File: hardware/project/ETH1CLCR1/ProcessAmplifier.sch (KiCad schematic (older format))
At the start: 87 parts, among them Q901 BC847W, Q902 BC847W, Q903 BC847W, U901 TL072, U902 TL072, U903 TL072, U904 TL072, U905 TL071, U906 TL071, U907 AQY212GS, U908 AQY212GS, U909 AQY212GS, U910 AQY212GS, U911 AQY212GS, U912 AQY212GS, U913 AQY212GS, U914 AQY212GS, U915 AQY212GS, U916 AQY212GS, U917 ULN2003A

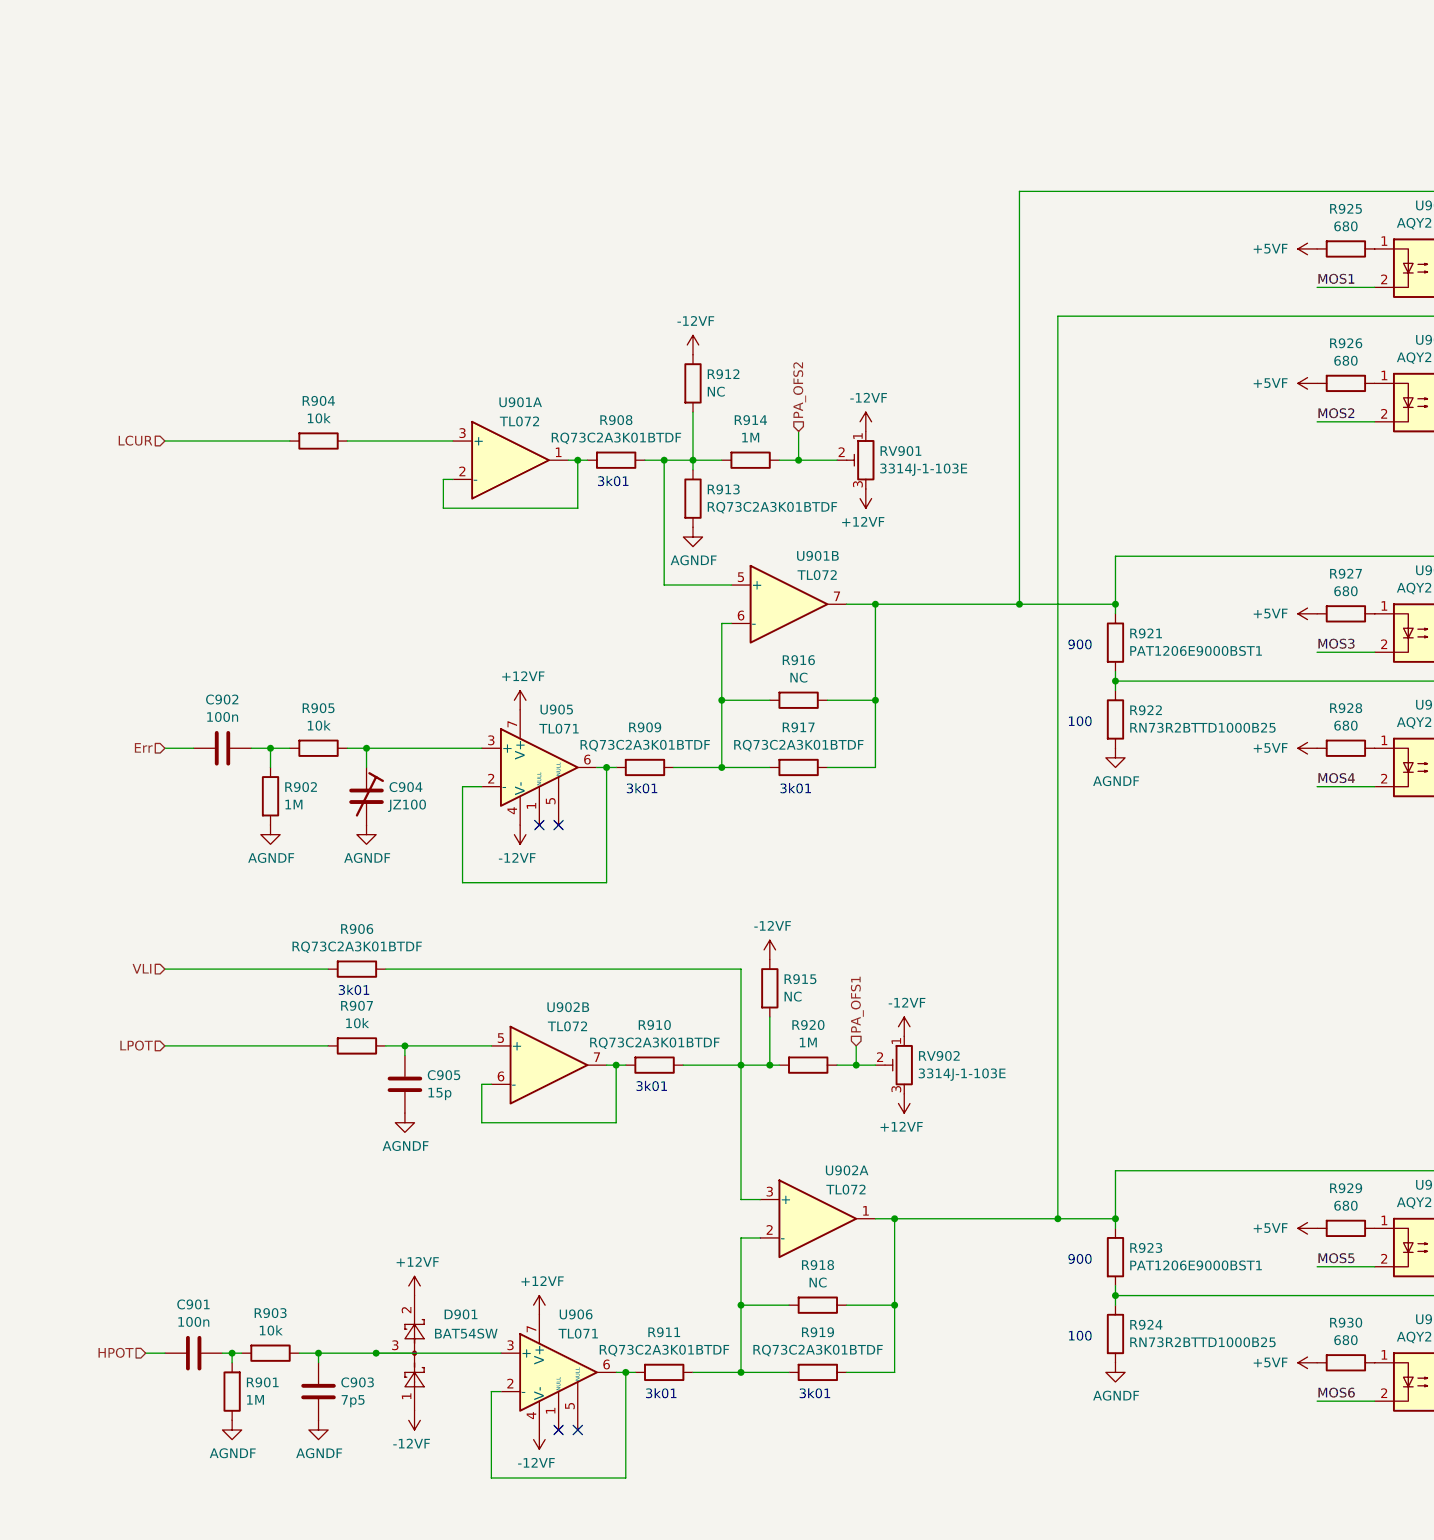
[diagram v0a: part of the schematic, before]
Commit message: Checked the schematics. Created BOM.
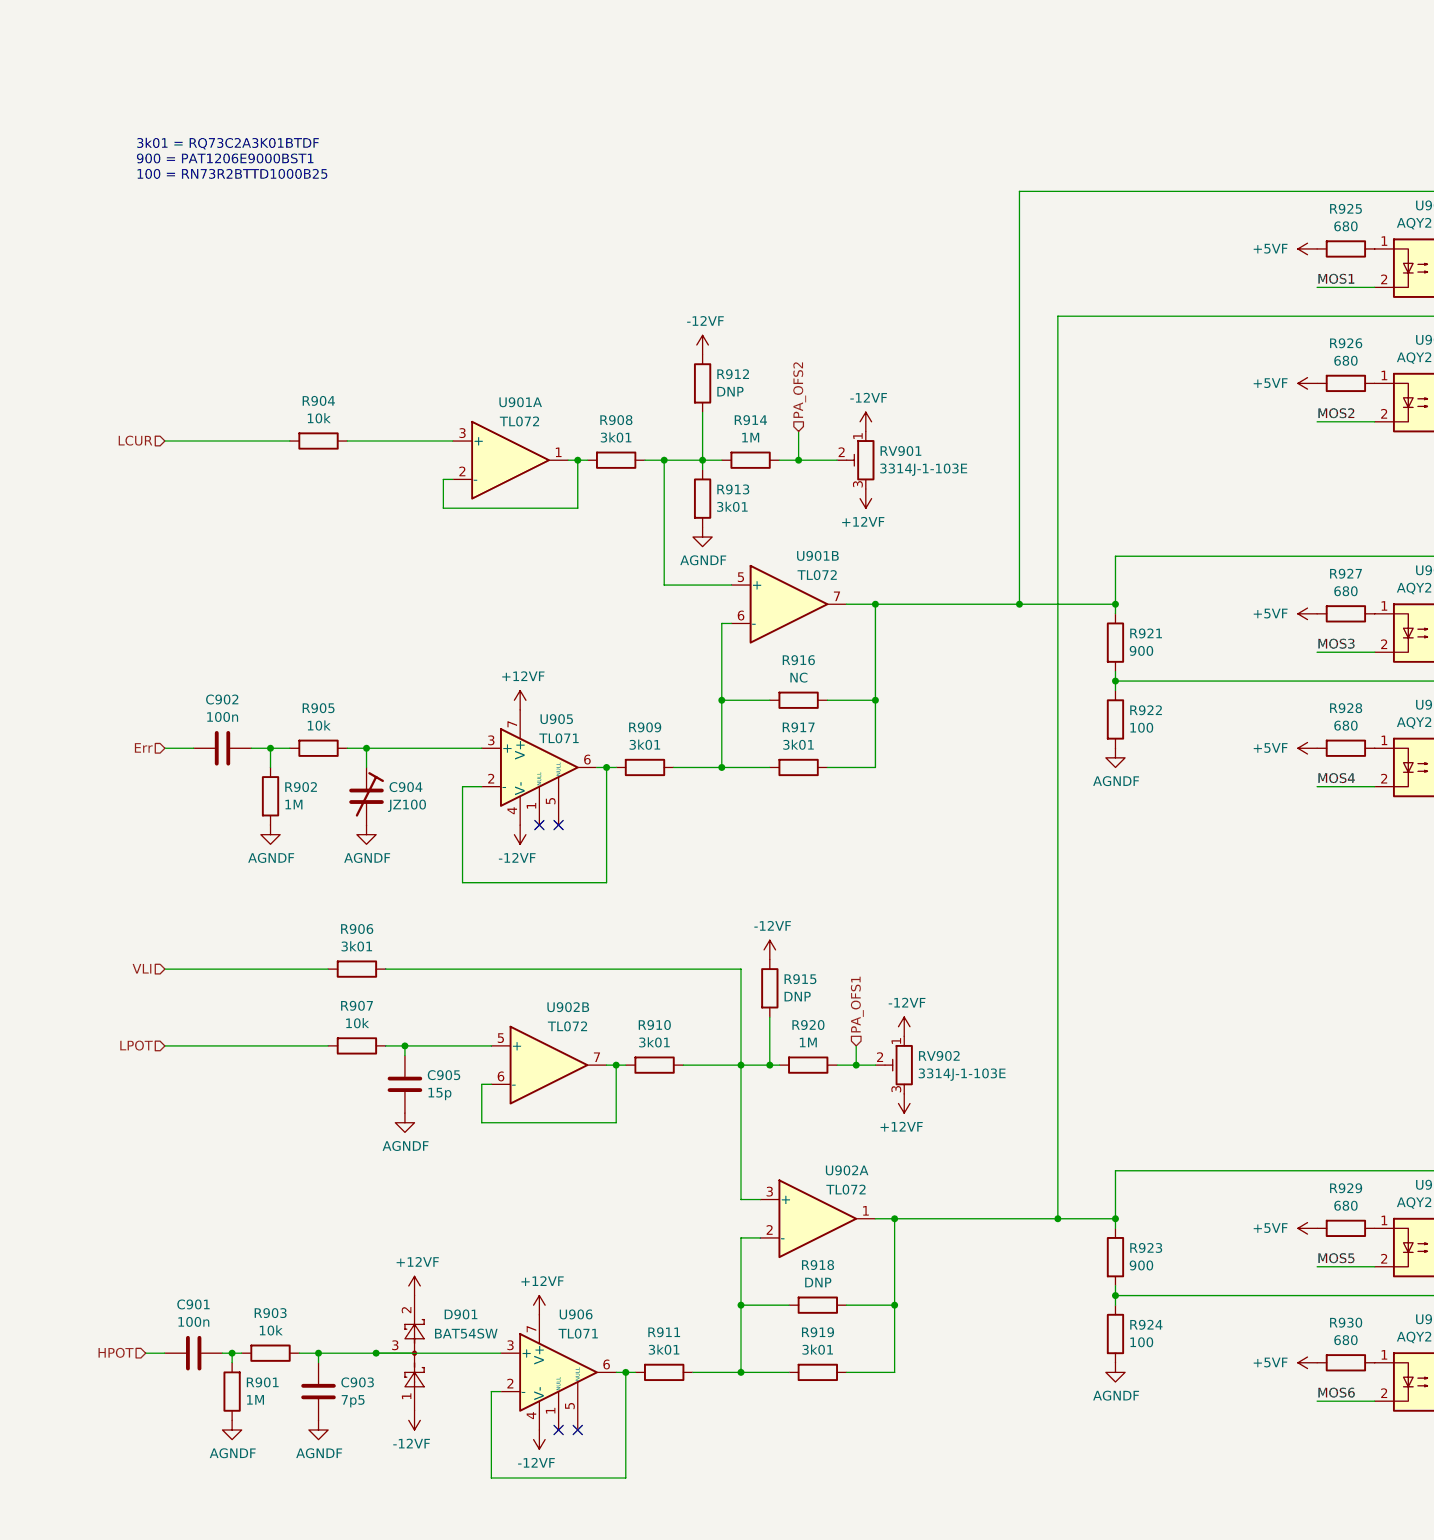
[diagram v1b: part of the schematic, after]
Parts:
- R906, R908, R909, R910, R911, R913, R917, R919: value RQ73C2A3K01BTDF -> 3k01
- R912, R915, R918: value NC -> DNP
- R921, R923: value PAT1206E9000BST1 -> 900
- R922, R924: value RN73R2BTTD1000B25 -> 100
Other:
- note added: "3k01 = RQ73C2A3K01BTDF\n900 = PAT1206E9000BST1\n100 = RN73R2BTTD1000B25"
- note removed: "100"
- note removed: "3k01"
- note removed: "900"
- moved on the sheet: R912, R913
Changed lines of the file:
@@
 P 4200 5300
 F 0 "R909" V 3993 5300 50  0000 C CNN
-F 1 "RQ73C2A3K01BTDF" V 4084 5300 50  0000 C CNN
+F 1 "3k01" V 4084 5300 50  0000 C CNN
 F 2 "Resistor_SMD:R_0805_2012Metric_Pad1.15x1.40mm_HandSolder" V 4130 5300 50  0001 C CNN
 F 3 "~" H 4200 5300 50  0001 C CNN
@@
 P 5000 5300
 F 0 "R917" V 4793 5300 50  0000 C CNN
-F 1 "RQ73C2A3K01BTDF" V 4884 5300 50  0000 C CNN
+F 1 "3k01" V 4884 5300 50  0000 C CNN
 F 2 "Resistor_SMD:R_0805_2012Metric_Pad1.15x1.40mm_HandSolder" V 4930 5300 50  0001 C CNN
 F 3 "~" H 5000 5300 50  0001 C CNN
@@
 L Device:R R913
 U 1 1 5EB670FA
-P 4450 3900
-F 0 "R913" H 4520 3946 50  0000 L CNN
-F 1 "RQ73C2A3K01BTDF" H 4520 3855 50  0000 L CNN
-F 2 "Resistor_SMD:R_0805_2012Metric_Pad1.15x1.40mm_HandSolder" V 4380 3900 50  0001 C CNN
-F 3 "~" H 4450 3900 50  0001 C CNN
-	1    4450 3900
+P 4500 3900
+F 0 "R913" H 4570 3946 50  0000 L CNN
+F 1 "3k01" H 4570 3855 50  0000 L CNN
+F 2 "Resistor_SMD:R_0805_2012Metric_Pad1.15x1.40mm_HandSolder" V 4430 3900 50  0001 C CNN
+F 3 "~" H 4500 3900 50  0001 C CNN
+	1    4500 3900
 	1    0    0    -1
 $EndComp
@@
 L ETH1CLCR1:AGNDF #PWR0921
 U 1 1 5EB67998
-P 4450 4050
-F 0 "#PWR0921" H 4450 3800 50  0001 C CNN
-F 1 "AGNDF" H 4455 3877 50  0000 C CNN
-F 2 "" H 4450 4050 50  0001 C CNN
-F 3 "" H 4450 4050 50  0001 C CNN
-	1    4450 4050
+P 4500 4050
+F 0 "#PWR0921" H 4500 3800 50  0001 C CNN
+F 1 "AGNDF" H 4505 3877 50  0000 C CNN
+F 2 "" H 4500 4050 50  0001 C CNN
+F 3 "" H 4500 4050 50  0001 C CNN
+	1    4500 4050
 	1    0    0    -1
 $EndComp
@@
 L Device:R R912
 U 1 1 5EB69155
-P 4450 3300
-F 0 "R912" H 4520 3346 50  0000 L CNN
-F 1 "NC" H 4520 3255 50  0000 L CNN
-F 2 "Resistor_SMD:R_0603_1608Metric_Pad1.05x0.95mm_HandSolder" V 4380 3300 50  0001 C CNN
-F 3 "~" H 4450 3300 50  0001 C CNN
-	1    4450 3300
-	1    0    0    -1
-$EndComp
-Wire Wire Line
-	4450 3450 4450 3700
+P 4500 3300
+F 0 "R912" H 4570 3346 50  0000 L CNN
+F 1 "DNP" H 4570 3255 50  0000 L CNN
+F 2 "Resistor_SMD:R_0603_1608Metric_Pad1.05x0.95mm_HandSolder" V 4430 3300 50  0001 C CNN
+F 3 "~" H 4500 3300 50  0001 C CNN
+	1    4500 3300
+	1    0    0    -1
+$EndComp
+Wire Wire Line
+	4500 3450 4500 3700
 $Comp
 L Device:R R908
@@
 P 4050 3700
 F 0 "R908" V 3843 3700 50  0000 C CNN
-F 1 "RQ73C2A3K01BTDF" V 3934 3700 50  0000 C CNN
+F 1 "3k01" V 3934 3700 50  0000 C CNN
 F 2 "Resistor_SMD:R_0805_2012Metric_Pad1.15x1.40mm_HandSolder" V 3980 3700 50  0001 C CNN
 F 3 "~" H 4050 3700 50  0001 C CNN
@@
 	3800 3700 3850 3700
 Wire Wire Line
-	4450 3700 4450 3750
+	4500 3700 4500 3750
 Wire Wire Line
 	4650 4350 4300 4350
@@
 Wire Wire Line
 	4300 3700 4200 3700
-Wire Wire Line
-	4300 3700 4450 3700
 Connection ~ 4300 3700
 Wire Wire Line
@@
 P 4850 6450
 F 0 "R915" H 4920 6496 50  0000 L CNN
-F 1 "NC" H 4920 6405 50  0000 L CNN
+F 1 "DNP" H 4920 6405 50  0000 L CNN
 F 2 "Resistor_SMD:R_0603_1608Metric_Pad1.05x0.95mm_HandSolder" V 4780 6450 50  0001 C CNN
 F 3 "~" H 4850 6450 50  0001 C CNN
@@
 P 5100 8100
 F 0 "R918" V 4893 8100 50  0000 C CNN
-F 1 "NC" V 4984 8100 50  0000 C CNN
+F 1 "DNP" V 4984 8100 50  0000 C CNN
 F 2 "Resistor_SMD:R_0603_1608Metric_Pad1.05x0.95mm_HandSolder" V 5030 8100 50  0001 C CNN
 F 3 "~" H 5100 8100 50  0001 C CNN
@@
 P 6650 5050
 F 0 "R922" H 6720 5096 50  0000 L CNN
-F 1 "RN73R2BTTD1000B25" H 6720 5005 50  0000 L CNN
+F 1 "100" H 6720 5005 50  0000 L CNN
 F 2 "Resistor_SMD:R_1206_3216Metric_Pad1.42x1.75mm_HandSolder" V 6580 5050 50  0001 C CNN
 F 3 "~" H 6650 5050 50  0001 C CNN
@@
 P 6650 4650
 F 0 "R921" H 6720 4696 50  0000 L CNN
-F 1 "PAT1206E9000BST1" H 6720 4605 50  0000 L CNN
+F 1 "900" H 6720 4605 50  0000 L CNN
 F 2 "Resistor_SMD:R_1206_3216Metric_Pad1.42x1.75mm_HandSolder" V 6580 4650 50  0001 C CNN
 F 3 "~" H 6650 4650 50  0001 C CNN
@@
 L ETH1CLCR1:-12VF #PWR0920
 U 1 1 5E5D6F64
-P 4450 3150
-F 0 "#PWR0920" H 4450 3000 50  0001 C CNN
-F 1 "-12VF" H 4465 3323 50  0000 C CNN
-F 2 "" H 4450 3150 50  0001 C CNN
-F 3 "" H 4450 3150 50  0001 C CNN
-	1    4450 3150
+P 4500 3150
+F 0 "#PWR0920" H 4500 3000 50  0001 C CNN
+F 1 "-12VF" H 4515 3323 50  0000 C CNN
+F 2 "" H 4500 3150 50  0001 C CNN
+F 3 "" H 4500 3150 50  0001 C CNN
+	1    4500 3150
 	1    0    0    -1
 $EndComp
@@
 P 2700 6350
 F 0 "R906" V 2493 6350 50  0000 C CNN
-F 1 "RQ73C2A3K01BTDF" V 2584 6350 50  0000 C CNN
+F 1 "3k01" V 2584 6350 50  0000 C CNN
 F 2 "Resistor_SMD:R_0805_2012Metric_Pad1.15x1.40mm_HandSolder" V 2630 6350 50  0001 C CNN
 F 3 "~" H 2700 6350 50  0001 C CNN
@@
 U 1 1 5E1A6D74
 P 3650 5300
-F 0 "U905" H 3650 5600 50  0000 L CNN
-F 1 "TL071" H 3650 5500 50  0000 L CNN
+F 0 "U905" H 3650 5550 50  0000 L CNN
+F 1 "TL071" H 3650 5450 50  0000 L CNN
 F 2 "Package_SO:SOIC-8_3.9x4.9mm_P1.27mm" H 3700 5350 50  0001 C CNN
 F 3 "http://www.ti.com/lit/ds/symlink/tl071.pdf" H 3800 5450 50  0001 C CNN
@@
 P 6650 8250
 F 0 "R924" H 6720 8296 50  0000 L CNN
-F 1 "RN73R2BTTD1000B25" H 6720 8205 50  0000 L CNN
+F 1 "100" H 6720 8205 50  0000 L CNN
 F 2 "Resistor_SMD:R_1206_3216Metric_Pad1.42x1.75mm_HandSolder" V 6580 8250 50  0001 C CNN
 F 3 "~" H 6650 8250 50  0001 C CNN
@@
 P 6650 7850
 F 0 "R923" H 6720 7896 50  0000 L CNN
-F 1 "PAT1206E9000BST1" H 6720 7805 50  0000 L CNN
+F 1 "900" H 6720 7805 50  0000 L CNN
 F 2 "Resistor_SMD:R_1206_3216Metric_Pad1.42x1.75mm_HandSolder" V 6580 7850 50  0001 C CNN
 F 3 "~" H 6650 7850 50  0001 C CNN
@@
 Wire Wire Line
 	6350 2950 8650 2950
-Text Notes 6400 4700 0    50   ~ 0
-900
-Text Notes 6400 5100 0    50   ~ 0
-100
-Text Notes 6400 7900 0    50   ~ 0
-900
-Text Notes 6400 8300 0    50   ~ 0
-100
 $Comp
 L Device:R R919
@@
 P 5100 8450
 F 0 "R919" V 4893 8450 50  0000 C CNN
-F 1 "RQ73C2A3K01BTDF" V 4984 8450 50  0000 C CNN
+F 1 "3k01" V 4984 8450 50  0000 C CNN
 F 2 "Resistor_SMD:R_0805_2012Metric_Pad1.15x1.40mm_HandSolder" V 5030 8450 50  0001 C CNN
 F 3 "~" H 5100 8450 50  0001 C CNN
@@
 P 4300 8450
 F 0 "R911" V 4093 8450 50  0000 C CNN
-F 1 "RQ73C2A3K01BTDF" V 4184 8450 50  0000 C CNN
+F 1 "3k01" V 4184 8450 50  0000 C CNN
 F 2 "Resistor_SMD:R_0805_2012Metric_Pad1.15x1.40mm_HandSolder" V 4230 8450 50  0001 C CNN
 F 3 "~" H 4300 8450 50  0001 C CNN
@@
 	0    1    1    0
 $EndComp
-Connection ~ 4450 3700
-Wire Wire Line
-	4450 3700 4600 3700
 $Comp
 L Device:R R910
@@
 P 4250 6850
 F 0 "R910" V 4043 6850 50  0000 C CNN
-F 1 "RQ73C2A3K01BTDF" V 4134 6850 50  0000 C CNN
+F 1 "3k01" V 4134 6850 50  0000 C CNN
 F 2 "Resistor_SMD:R_0805_2012Metric_Pad1.15x1.40mm_HandSolder" V 4180 6850 50  0001 C CNN
 F 3 "~" H 4250 6850 50  0001 C CNN
@@
 Wire Wire Line
 	4700 6850 4700 7550
-Text Notes 4150 7000 0    50   ~ 0
-3k01
-Text Notes 5000 8600 0    50   ~ 0
-3k01
-Text Notes 4200 8600 0    50   ~ 0
-3k01
-Text Notes 2600 6500 0    50   ~ 0
-3k01
-Text Notes 3950 3850 0    50   ~ 0
-3k01
-Text Notes 4100 5450 0    50   ~ 0
-3k01
-Text Notes 4900 5450 0    50   ~ 0
-3k01
+Text Notes 1550 2250 0    50   ~ 0
+3k01 = RQ73C2A3K01BTDF\n900 = PAT1206E9000BST1\n100 = RN73R2BTTD1000B25
 $Comp
 L Transistor_Array:ULN2003A U917
@@
 	-1   0    0    -1
 $EndComp
+Connection ~ 4500 3700
+Wire Wire Line
+	4500 3700 4600 3700
+Wire Wire Line
+	4300 3700 4500 3700
 $EndSCHEMATC
